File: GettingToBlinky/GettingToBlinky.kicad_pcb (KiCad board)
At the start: 2 copper layers, 6 parts, among them U1 7555

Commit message: finished pcb layout
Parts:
- added BT1: Battery, GTB:BatteryHolder, B.Cu at (213.4, 128.9)
- moved C1 80.0 mm to (222.2, 135.9), turned to 270 degrees
- moved R2 77.0 mm to (222.2, 127.0), turned to 270 degrees
- moved R1 74.7 mm to (222.2, 116.8), turned to 270 degrees
- moved D1 73.5 mm to (214.6, 137.2), turned to 180 degrees
- moved U1 68.5 mm to (213.4, 127.0)
- moved R3 66.5 mm to (207.0, 136.5), turned to 270 degrees
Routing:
- net /VDD: track 0.00 -> 18.8 mm, vias 0 -> 2
- net Net-(C1-Pad1): track 0.00 -> 18.0 mm
- net Net-(R1-Pad2): track 0.00 -> 13.9 mm
- net Net-(R3-Pad1): track 0.00 -> 11.5 mm
- net GND: track 0.00 -> 9.20 mm, vias 0 -> 1
- net Net-(D1-Pad2): track 0.00 -> 5.42 mm
- added copper zone on B.Cu, net /VDD
- added copper zone on F.Cu, net GND
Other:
- board outline added: 35.6 x 35.6 mm
- net class Default: clearance 0.2 -> 0.254; trace_width 0.25 -> 0.254; via_dia 0.6 -> 0.6858; via_drill 0.4 -> 0.3302
- rule trace_clearance: 0.2 -> 0.254
- rule trace_min: 0.2 -> 0.1524
- rule via_min_drill: 0.3 -> 0.3302
- rule via_min_size: 0.4 -> 0.6858
- board text added: "Getting to Blinky © Axello"

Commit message: Created gerber files
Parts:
- moved R1 0.63 mm to (222.2, 117.5)
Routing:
- net /VDD: track 18.8 -> 18.1 mm
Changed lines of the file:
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@@
     (visible_elements FFFFF77F)
     (pcbplotparams
-      (layerselection 0x00030_80000001)
+      (layerselection 0x010f0_80000001)
       (usegerberextensions false)
       (excludeedgelayer true)
@@
       (psa4output false)
       (plotreference true)
-      (plotvalue true)
+      (plotvalue false)
       (plotinvisibletext false)
       (padsonsilk false)
-      (subtractmaskfromsilk false)
+      (subtractmaskfromsilk true)
       (outputformat 1)
       (mirror false)
-      (drillshape 1)
+      (drillshape 0)
       (scaleselection 1)
-      (outputdirectory ""))
+      (outputdirectory Gerbers/))
   )
   (net 0 "")
@@
   )
   (module Resistors_SMD:R_0805_HandSoldering (layer F.Cu)
-    (at 222.25 116.84 270)
+    (at 222.25 117.475 270)
     (descr "Resistor SMD 0805, hand soldering")
     (tags "resistor 0805")
@@
   (segment (start 216.06 125.095) (end 216.06 124.935) (width 0.254) (layer F.Cu) (net 4))
   (segment (start 216.06 124.935) (end 219.71 121.285) (width 0.254) (layer F.Cu) (net 4))
-  (segment (start 219.71 121.285) (end 219.71 116.205) (width 0.254) (layer F.Cu) (net 4))
-  (segment (start 219.71 116.205) (end 220.425 115.49) (width 0.254) (layer F.Cu) (net 4))
-  (segment (start 220.425 115.49) (end 222.25 115.49) (width 0.254) (layer F.Cu) (net 4))
+  (segment (start 219.71 121.285) (end 219.71 116.84) (width 0.254) (layer F.Cu) (net 4))
+  (segment (start 219.71 116.84) (end 220.425 116.125) (width 0.254) (layer F.Cu) (net 4))
+  (segment (start 220.425 116.125) (end 222.25 116.125) (width 0.254) (layer F.Cu) (net 4))
   (segment (start 216.06 126.365) (end 220.345 126.365) (width 0.254) (layer F.Cu) (net 5))
-  (segment (start 221.06 125.65) (end 222.25 125.65) (width 0.254) (layer F.Cu) (net 5))
+  (segment (start 221.06 125.65) (end 222.25 126.285) (width 0.254) (layer F.Cu) (net 5))
   (segment (start 220.345 126.365) (end 221.06 125.65) (width 0.254) (layer F.Cu) (net 5))
-  (segment (start 222.25 125.65) (end 222.25 118.19) (width 0.254) (layer F.Cu) (net 5))
+  (segment (start 222.25 126.285) (end 222.25 118.825) (width 0.254) (layer F.Cu) (net 5))
   (segment (start 207.01 135.81) (end 207.01 128.27) (width 0.254) (layer F.Cu) (net 6))
   (segment (start 207.645 127.635) (end 210.66 127.635) (width 0.254) (layer F.Cu) (net 6))

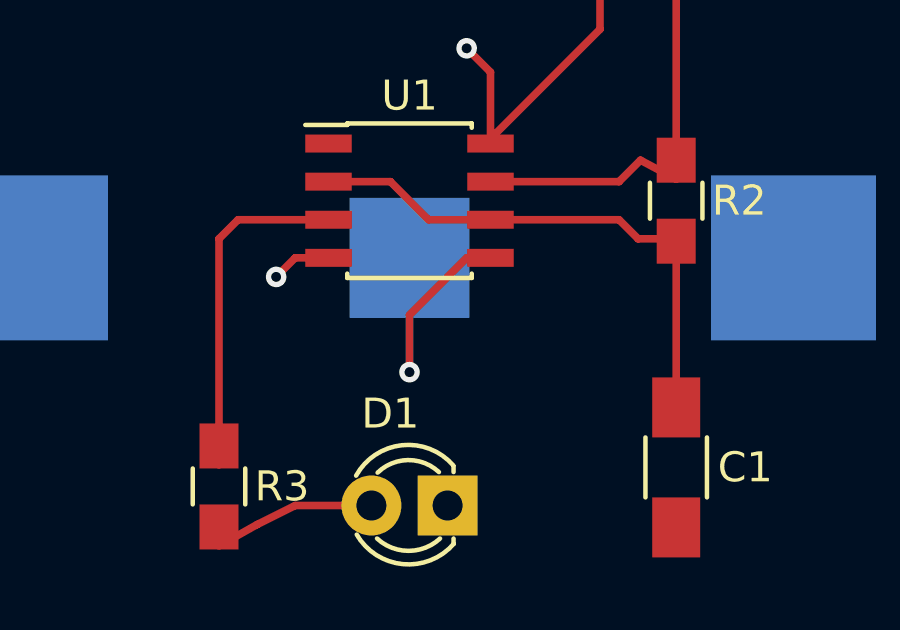
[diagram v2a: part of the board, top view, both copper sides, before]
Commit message: removed pin5 connection, re-generated pcb
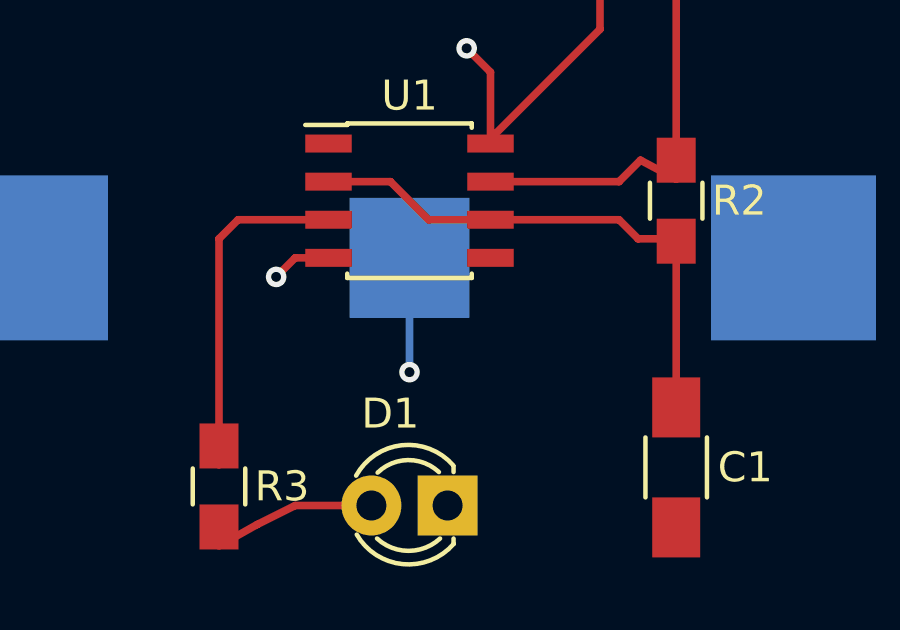
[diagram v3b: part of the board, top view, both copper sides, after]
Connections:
- U1 pad 5: GND -> Net-(U1-Pad5)
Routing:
- net GND: track 9.20 -> 3.81 mm
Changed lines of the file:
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@@
 (kicad_pcb (version 4) (host pcbnew 4.0.6)
   (general
-    (links 15)
+    (links 14)
     (no_connects 0)
     (area 195.504999 110.414999 231.215001 146.125001)
     (thickness 1.6)
     (drawings 5)
-    (tracks 35)
+    (tracks 31)
     (zones 0)
     (modules 7)
-    (nets 7)
+    (nets 8)
   )
   (page A4)
   (layers
     (0 F.Cu signal)
-    (31 B.Cu signal)
+    (31 B.Cu signal hide)
     (32 B.Adhes user)
     (33 F.Adhes user)
@@
     (pad_to_mask_clearance 0.2)
     (aux_axis_origin 0 0)
-    (visible_elements FFFFF77F)
+    (visible_elements FFFC422F)
     (pcbplotparams
       (layerselection 0x010f0_80000001)
@@
   (net 5 "Net-(R1-Pad2)")
   (net 6 "Net-(R3-Pad1)")
+  (net 7 "Net-(U1-Pad5)")
   (net_class Default "This is the default net class."
     (clearance 0.254)
@@
     (add_net "Net-(R1-Pad2)")
     (add_net "Net-(R3-Pad1)")
+    (add_net "Net-(U1-Pad5)")
   )
   (module GTB:BatteryHolder (layer B.Cu)
     (at 213.36 128.905)
-    (fp_text reference BT1 (at 0 8.89) (layer B.SilkS)
+    (fp_text reference BT1 (at -3.175 3.81) (layer B.SilkS)
       (effects (font (size 1 1) (thickness 0.15)) (justify mirror))
     )
@@
       (net 4 /VDD))
     (pad 5 smd rect (at 2.7 1.905) (size 1.55 0.6) (layers F.Cu F.Paste F.Mask)
-      (net 2 GND))
+      (net 7 "Net-(U1-Pad5)"))
     (pad 6 smd rect (at 2.7 0.635) (size 1.55 0.6) (layers F.Cu F.Paste F.Mask)
       (net 1 "Net-(C1-Pad1)"))
@@
   (segment (start 213.36 128.905) (end 213.36 132.715) (width 0.254) (layer B.Cu) (net 2))
   (via (at 213.36 132.715) (size 0.6858) (drill 0.3302) (layers F.Cu B.Cu) (net 2))
-  (segment (start 213.36 130.81) (end 213.36 132.715) (width 0.254) (layer F.Cu) (net 2))
-  (segment (start 215.265 128.905) (end 213.995 130.175) (width 0.254) (layer F.Cu) (net 2))
-  (segment (start 213.995 130.175) (end 213.36 130.81) (width 0.254) (layer F.Cu) (net 2))
-  (segment (start 215.265 128.905) (end 216.06 128.905) (width 0.254) (layer F.Cu) (net 2))
   (segment (start 212.09 137.16) (end 209.55 137.16) (width 0.254) (layer F.Cu) (net 3))
   (segment (start 208.28 137.795) (end 207.01 138.51) (width 0.254) (layer F.Cu) (net 3))
